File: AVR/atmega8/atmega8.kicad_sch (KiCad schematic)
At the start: 9 parts, among them U1 ATmega8-16AU-MCU_Microchip_AT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

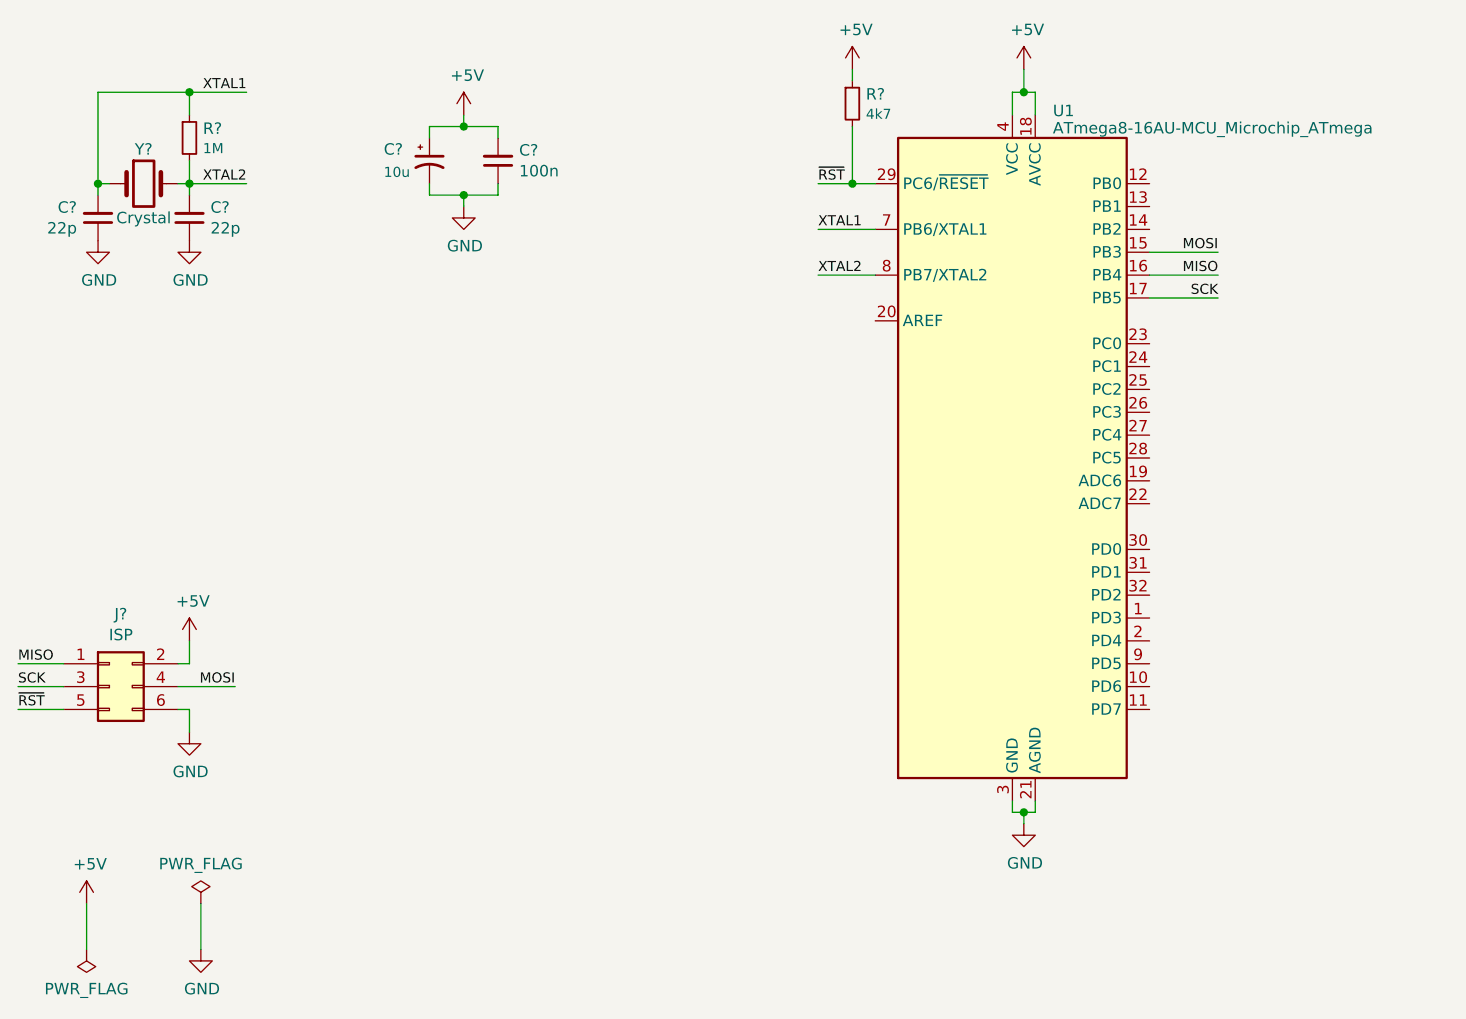
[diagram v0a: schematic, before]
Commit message: Fix grid alignment and update to KiCad 9
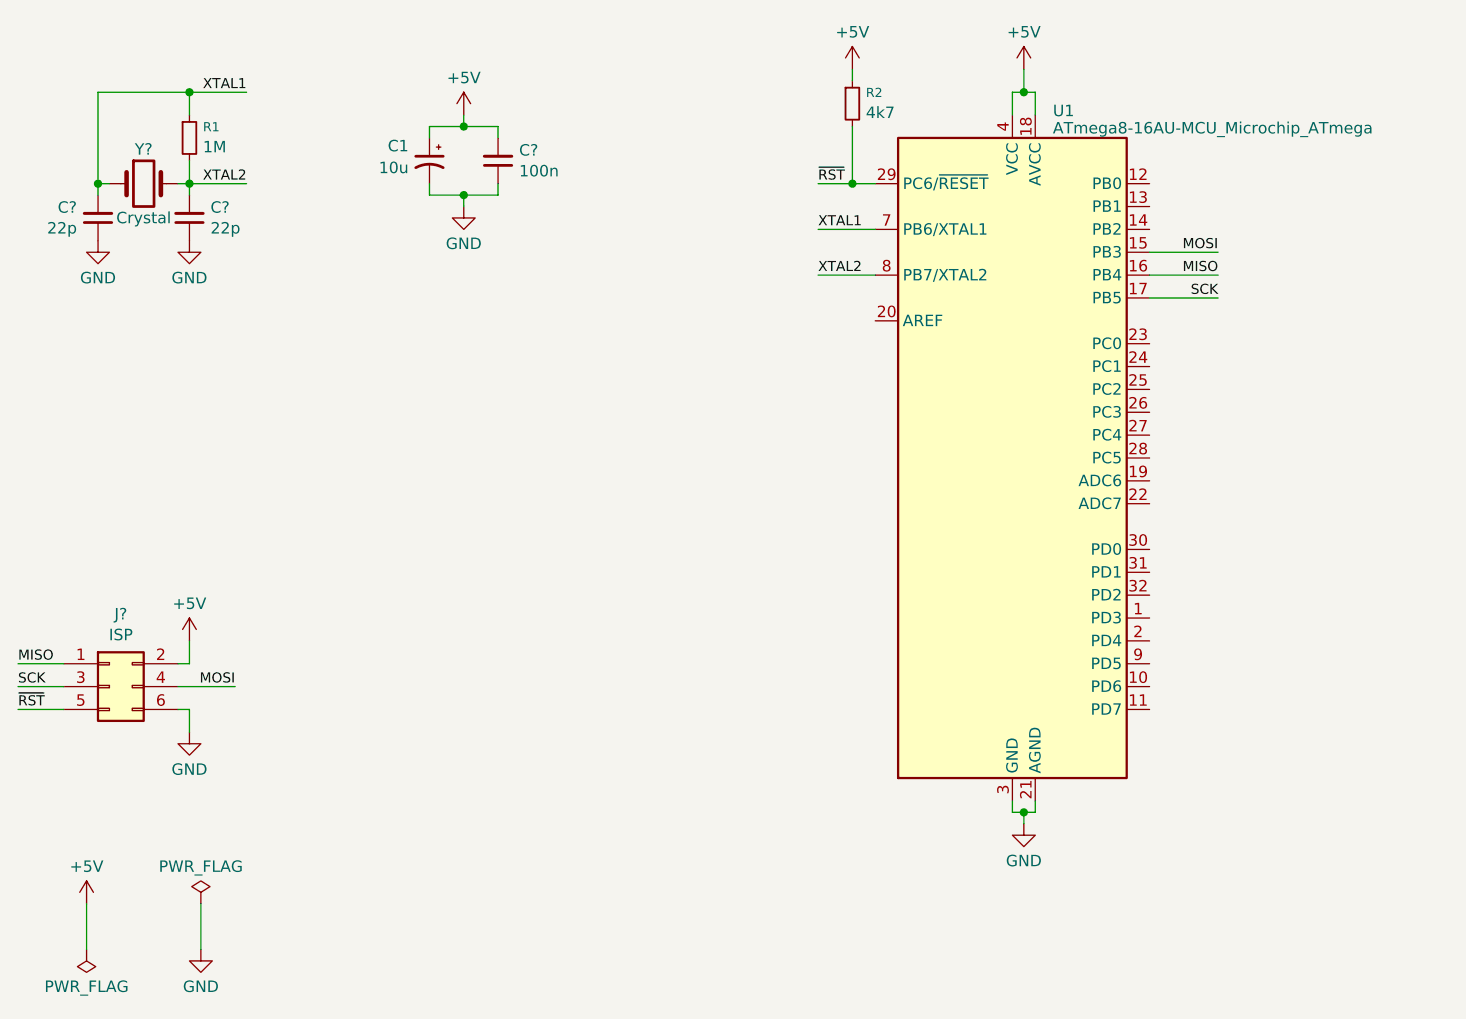
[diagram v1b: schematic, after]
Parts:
- removed C?: 22p, symbol Device:C_Small
- removed C?: 100n, symbol Device:C_Small
- removed C?: 10u, symbol Device:CP1_Small
- removed R?: 1M, symbol Device:R_Small
- removed R?: 4k7, symbol Device:R_Small
- added C1: 10u, symbol Device:C_Polarized_Small_US
- added C?: 100n, symbol Device:C_Small
- added C?: 22p, symbol Device:C_Small
- added R1: 1M, symbol Device:R_Small
- added R2: 4k7, symbol Device:R_Small
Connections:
- net +5V: now also C1.1, C?.2, R2.1
- net GND: now also C1.2, C?.1, C?.1
- net XTAL1: now also C?.2, R1.1
- net XTAL2: now also R1.2
- net ~{RST}: now also R2.2
